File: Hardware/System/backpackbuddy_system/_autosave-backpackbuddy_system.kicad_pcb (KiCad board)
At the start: 2 copper layers, 65 x 56 mm, 76 parts, among them J1 PIR, J10 USB_B_Micro, J11 Battery, J2 Ultrasonic 2, J3 Ultrasonic 1, J4 Left Vibration 1, J5 Left Vibration 2, J6 RPi_GPIO, J7 ESP8266, J8 Right Vibration 1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

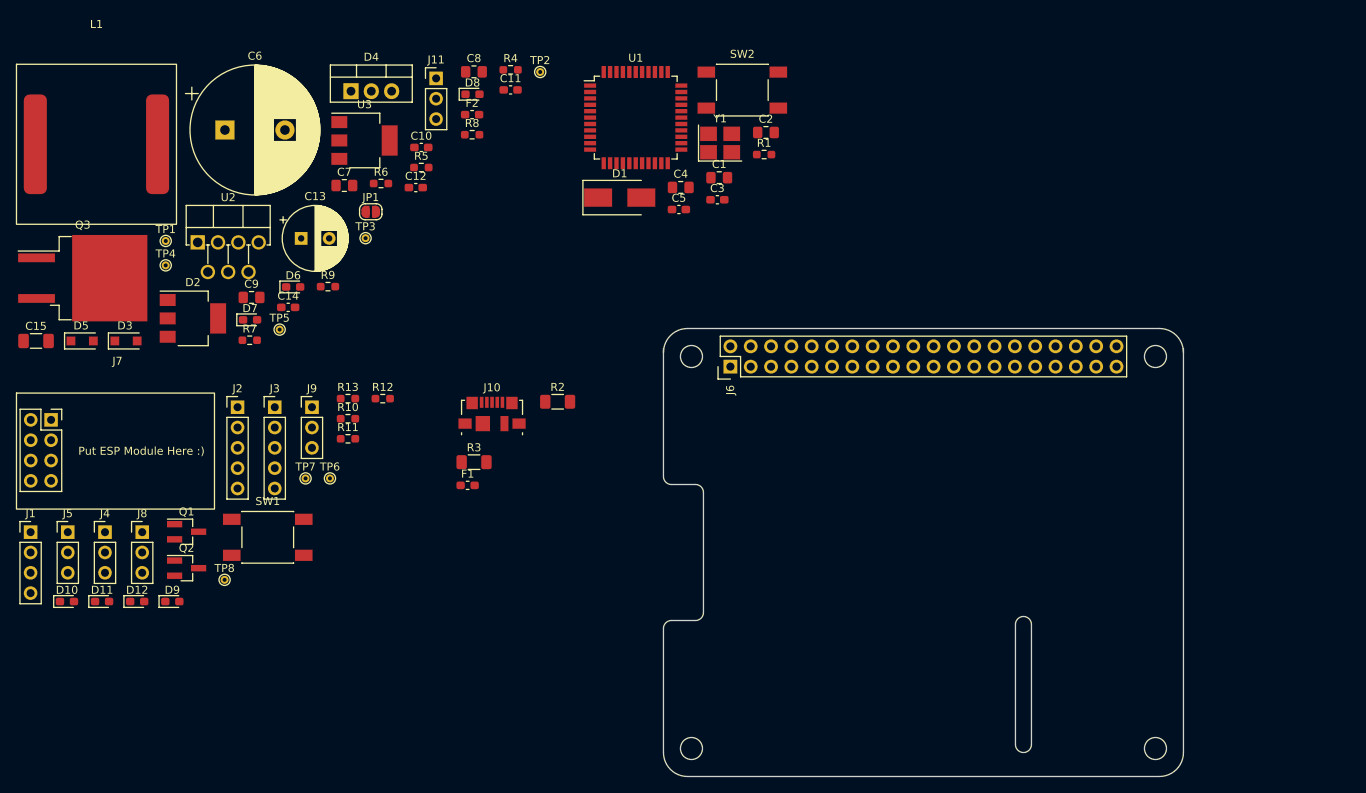
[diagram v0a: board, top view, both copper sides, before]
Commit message: pull down resistor to ESP reset
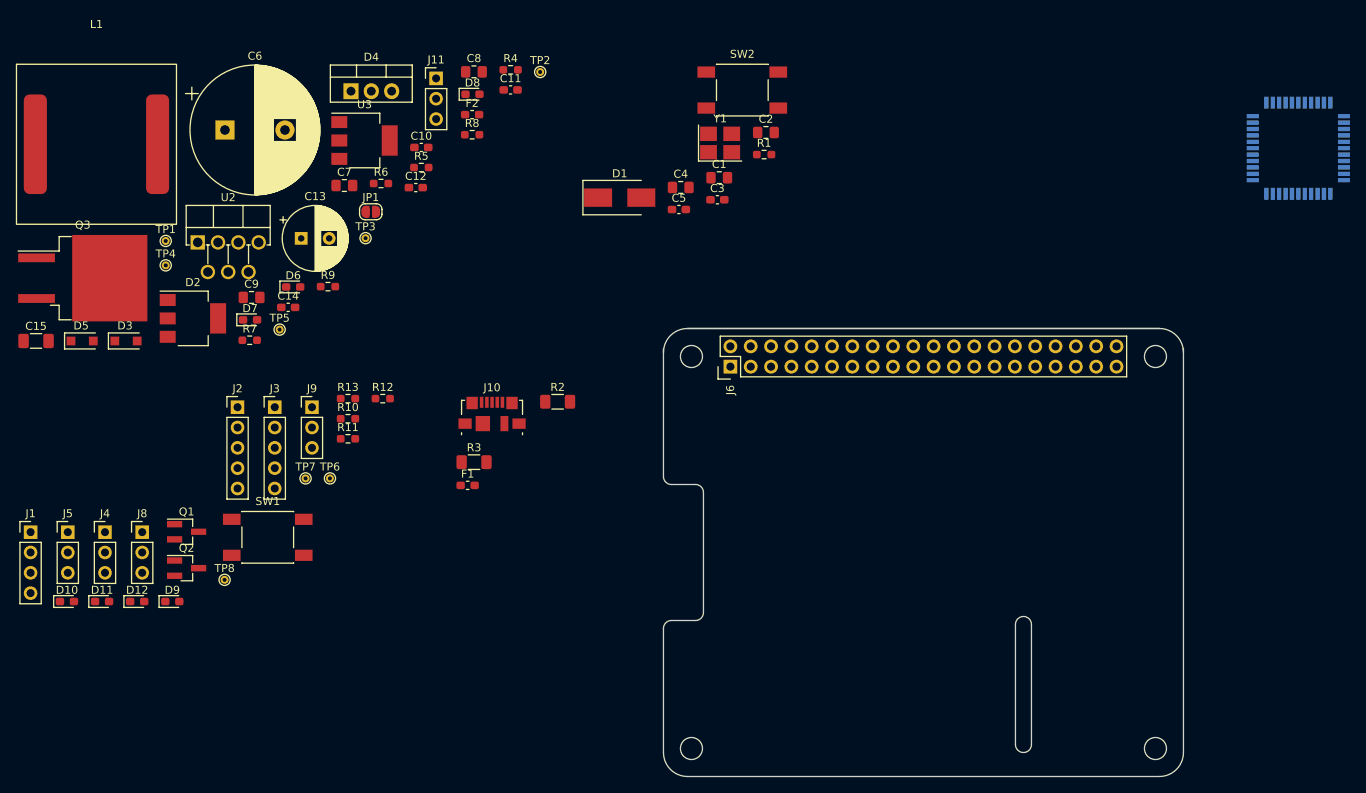
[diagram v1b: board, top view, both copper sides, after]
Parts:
- removed J7: ESP8266, BackpackBuddyFootprintLibrary:ESP8266
- U1: moved to B.Cu
- moved U1 82.9 mm to (190.4, 37.5), turned to 180 degrees

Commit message: decoupling caps
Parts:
- added J7: ESP8266, BackpackBuddyFootprintLibrary:ESP8266, F.Cu at (110.5, 94.0)
- added R14: 10k, Resistor_SMD:R_0603_1608Metric_Pad0.98x0.95mm_HandSolder, F.Cu at (125.7, 79.2)
- C1, C2, L1, Y1: moved to B.Cu
- moved J1 130.4 mm to (159.2, 113.8), turned to 90 degrees
- moved U2 109.7 mm to (160.0, 72.4)
- moved C13 108.4 mm to (166.4, 88.9)
- moved D4 103.1 mm to (161.3, 81.8)
- moved J11 99.9 mm to (173.6, 69.9)
- moved C6 97.9 mm to (145.1, 76.2)
- moved D9 95.6 mm to (144.8, 102.9)
- moved D12 94.9 mm to (139.7, 102.9)
- moved D11 94.2 mm to (134.6, 102.9)
- moved D10 93.5 mm to (129.5, 102.9)
- moved J2 93.0 mm to (139.7, 113.8), turned to 90 degrees
- moved J10 87.5 mm to (171.4, 101.6), turned to 90 degrees
- moved J5 84.2 mm to (119.4, 100.3)
- moved R10 78.7 mm to (144.8, 100.3)
- moved R13 75.1 mm to (139.7, 100.3)
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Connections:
- J6 pad 1: /Raspberry Pi/3v3 -> +3V3
- J6 pad 14: /Raspberry Pi/gnd -> GND
- J6 pad 17: /Raspberry Pi/3v3 -> +3V3
- J6 pad 2: /Raspberry Pi/5v -> +5V
- J6 pad 20: /Raspberry Pi/gnd -> GND
- J6 pad 25: /Raspberry Pi/gnd -> GND
- J6 pad 3: unconnected-(J6-Pad3) -> /Raspberry Pi/GPIO2_SDA
- J6 pad 30: /Raspberry Pi/gnd -> GND
- J6 pad 34: /Raspberry Pi/gnd -> GND
- J6 pad 39: /Raspberry Pi/gnd -> GND
- J6 pad 4: /Raspberry Pi/5v -> +5V
- J6 pad 5: unconnected-(J6-Pad5) -> /Raspberry Pi/GPIO3_SCL
- J6 pad 6: /Raspberry Pi/gnd -> GND
- J6 pad 7: unconnected-(J6-Pad7) -> /Raspberry Pi/GPIO4_GPCLK0
- J6 pad 9: /Raspberry Pi/gnd -> GND
- SW1 pad 2: GND -> +3V3
